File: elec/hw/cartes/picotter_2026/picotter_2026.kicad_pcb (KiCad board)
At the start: 4 copper layers, 100.5 x 87 mm, 175 parts, among them J10 22053051, J11 22272041, J12 22272051, J13 5264-3P, J14 22053051, J15 22053051, J16 22272041, J17 22272051, J18 2-1445051-3, J2 Conn_ARM_SWD_TagConnect_TC2030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

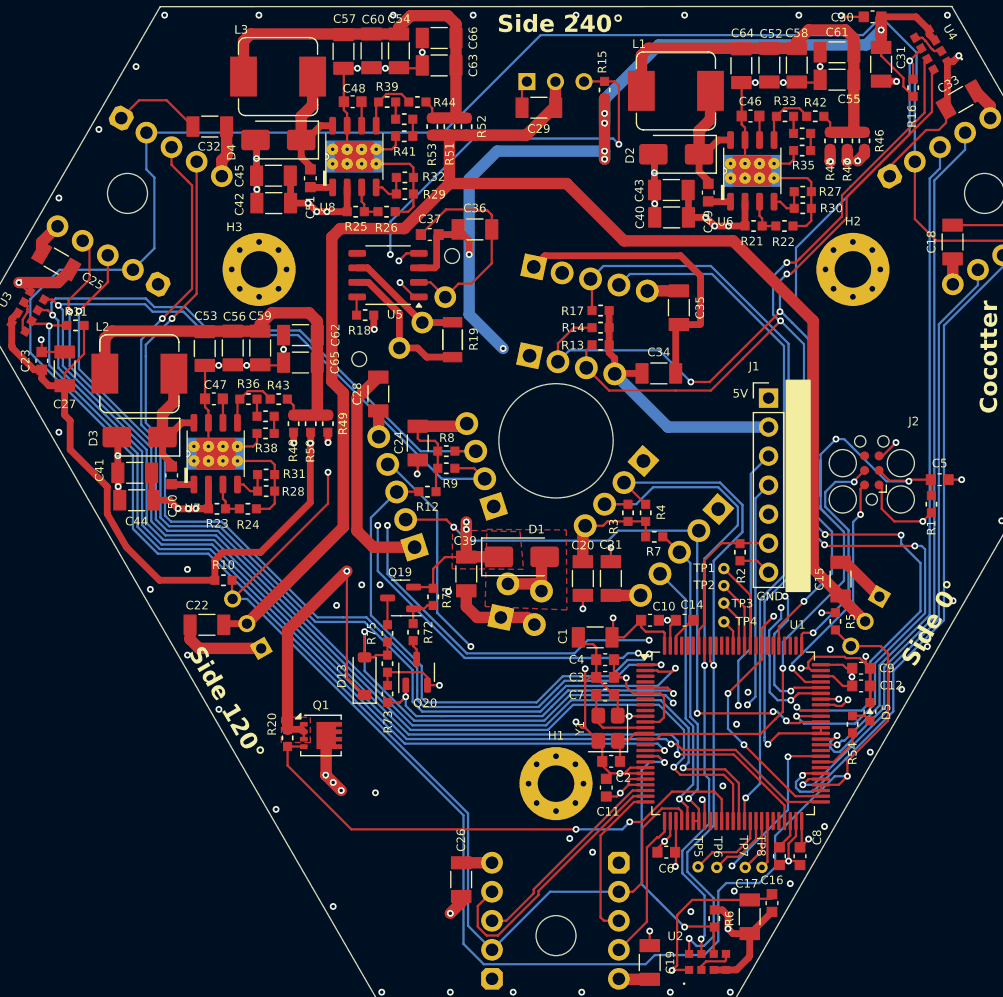
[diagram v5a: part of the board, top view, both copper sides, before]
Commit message: picotter: 3v3 to 5v translator added to neopixel cmd signal. schematic and pcb modified.
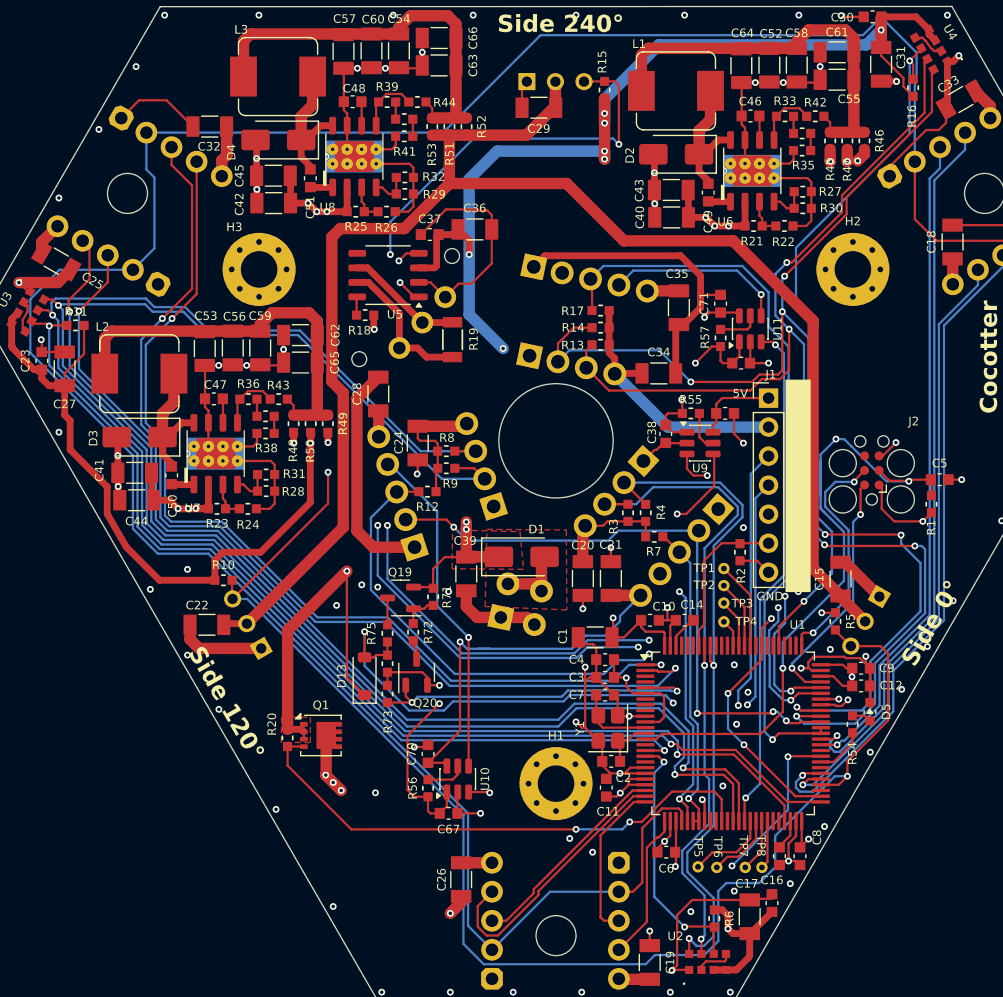
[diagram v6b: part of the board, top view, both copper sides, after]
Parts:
- added C38: 100nF 50V, cocotter_capacitors:C_0603_1608Metric, F.Cu at (159.6, 99.4)
- added C67: 100nF 50V, cocotter_capacitors:C_0603_1608Metric, F.Cu at (140.6, 132.6)
- added C68: 100nF 50V, cocotter_capacitors:C_0603_1608Metric, F.Cu at (166.2, 93.2)
- added C69: 100nF 50V, cocotter_capacitors:C_0603_1608Metric, F.Cu at (164.8, 97.6)
- added C70: 100nF 50V, cocotter_capacitors:C_0603_1608Metric, F.Cu at (138.8, 127.4)
- added C71: 100nF 50V, cocotter_capacitors:C_0603_1608Metric, F.Cu at (164.4, 88.0)
- added R55: 10k 1%, cocotter_resistor:r0603_reflow, F.Cu at (161.8, 97.6)
- added R56: 10k 1%, cocotter_resistor:r0603_reflow, F.Cu at (138.8, 130.4)
- added R57: 10k 1%, cocotter_resistor:r0603_reflow, F.Cu at (164.4, 91.0)
- added U10: SN74LVC1T45DBV, Package_TO_SOT_SMD:SOT-23-6, F.Cu at (141.4, 129.6)
- added U11: SN74LVC1T45DBV, Package_TO_SOT_SMD:SOT-23-6, F.Cu at (167.0, 90.2)
- added U9: SN74LVC1T45DBV, Package_TO_SOT_SMD:SOT-23-6, F.Cu at (162.6, 100.2)
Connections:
- J12 pad 4: /Side 120/neopixel_cmd_3v3 -> /Side 120/neopixel_cmd_5v
- J17 pad 4: /Side 240/neopixel_cmd_3v3 -> /Side 240/neopixel_cmd_5v
- J7 pad 4: /Side 0/neopixel_cmd_3v3 -> /Side 0/neopixel_cmd_5v
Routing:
- net +5V: track 104.9 -> 147.8 mm, vias 3 -> 5
- net /Side 120/neopixel_cmd_3v3: track 72.4 -> 41.7 mm
- net /Side 120/neopixel_cmd_5v: track 0.00 -> 29.5 mm, vias 0 -> 1
- net +3.3V: track 474.4 -> 502.6 mm, vias 20 -> 23
- net GND: track 325.8 -> 344.1 mm, vias 88 -> 96
- net /Side 240/neopixel_cmd_5v: track 0.00 -> 15.7 mm, vias 0 -> 1
- net /Side 240/neopixel_cmd_3v3: track 60.5 -> 44.8 mm, vias 1 -> 2
- net /Side 0/neopixel_cmd_3v3: track 23.6 -> 39.2 mm, vias 1 -> 3
- net /Side 0/neopixel_cmd_5v: track 0.00 -> 13.0 mm, vias 0 -> 1
- net /Side 120/digital_servo_cmd_3v3: track 78.9 -> 73.4 mm
- net Net-(U11-DIR): track 0.00 -> 3.64 mm
- net /Side 240/lidar_rx_0_3v3: track 88.4 -> 84.9 mm
- net Net-(U10-DIR): track 0.00 -> 3.52 mm
- net /Side 240/lidar_tx_0_3v3: track 93.8 -> 90.3 mm
- net Net-(U9-DIR): track 0.00 -> 3.48 mm
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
